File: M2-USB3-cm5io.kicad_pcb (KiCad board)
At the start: 4 copper layers, 23.7 x 80.1 mm, 53 parts, among them J1 Bus_M.2_Socket_M, J2 Conn_01x16_MountingPin, J3 Conn_01x16_MountingPin, J4 USB3_A, U1 VL805, U18 MP3422GG-P, U2 W25Q32JVZP, U4 TLV62568ADRLR, Y1 25Mhz

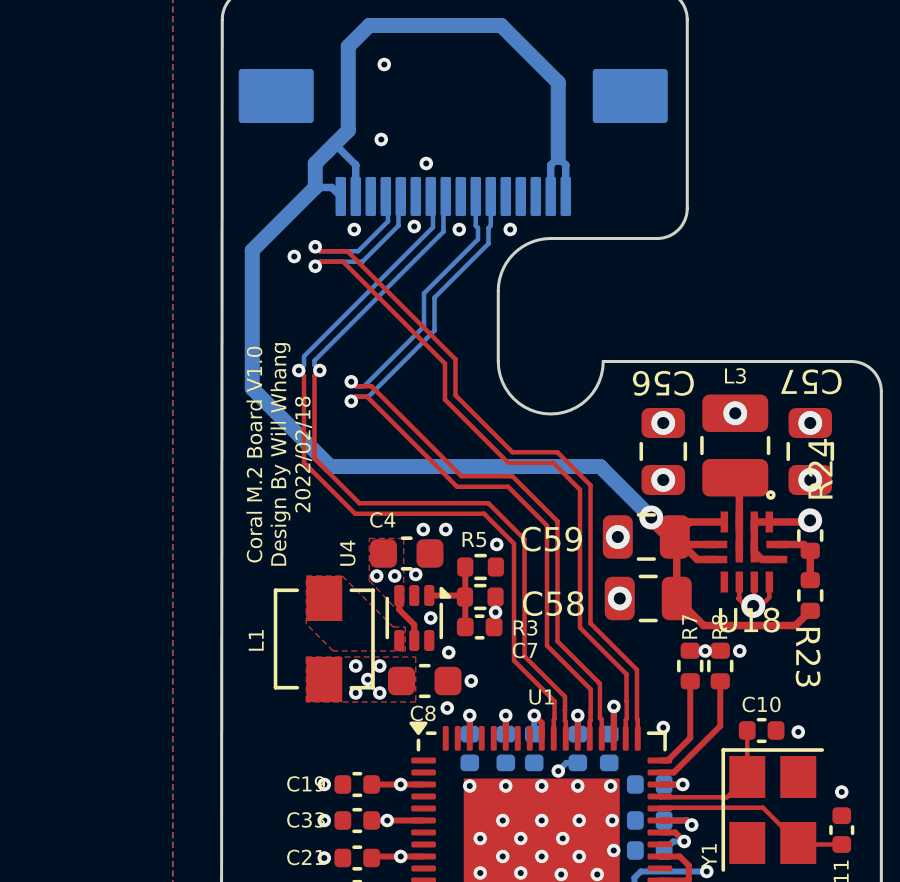
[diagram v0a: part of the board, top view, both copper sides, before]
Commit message: Change some components to things I already have in stock
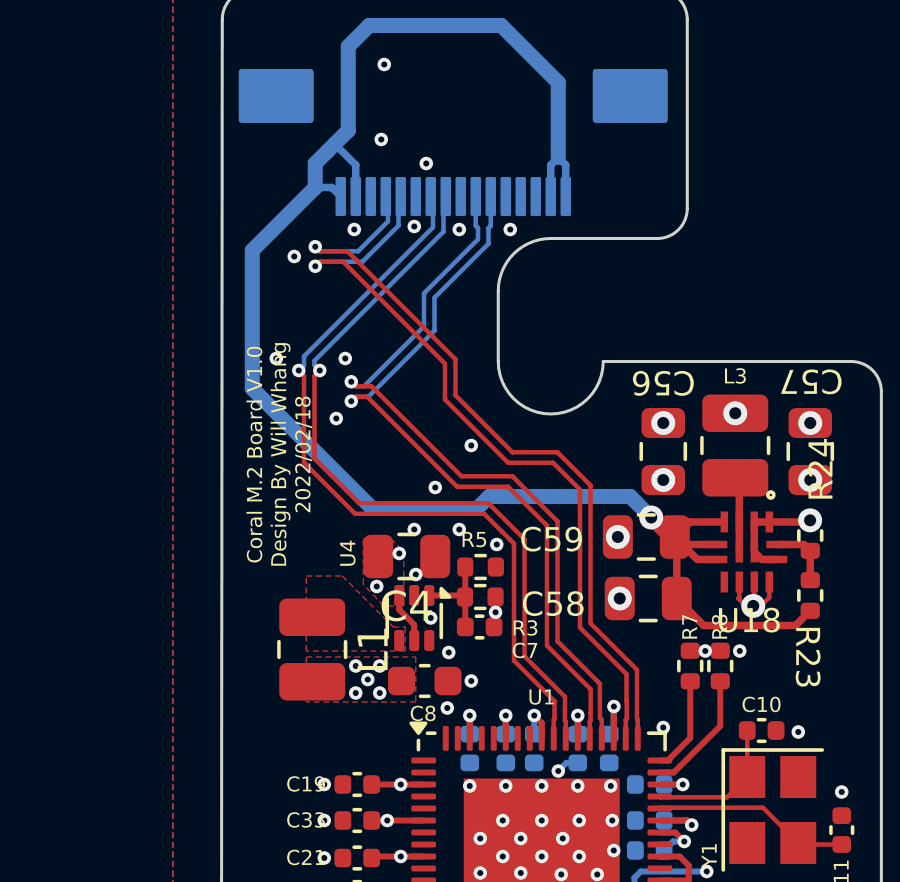
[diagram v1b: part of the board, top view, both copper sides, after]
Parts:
- C10: value 18pF -> 10pf
- C4: footprint Capacitor_SMD:C_0603_1608Metric -> Capacitor_SMD:C_0805_2012Metric
- L1: footprint Inductor_SMD:L_Vishay_IHLP-1212 -> Inductor_SMD:L_1008_2520Metric
- R11: value 15K -> 10k
- moved L1 0.53 mm to (104.2, 109.1)
- moved C4 0.10 mm to (107.3, 106.0)
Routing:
- net GND: vias 85 -> 90
